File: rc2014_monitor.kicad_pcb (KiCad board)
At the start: 2 copper layers, 99.1 x 49.9 mm, 51 parts, among them J1 Z80 Bus, J2 Pro Bus, J3 USB_B_Micro, J4 M3 Mounting Hole, SW1 Line Selection, SW2 SW_Push, SW3 Step, SW4 Run/Step Mode, U1 74HCT138, U10 LMC555xM, U11 74HCT00, U12 74HCT74, U2 74HCT151, U3 74HCT541, U4 74HCT541, U5 74HCT541, U6 74HCT32, U7 MAX40200AUK, U8 MAX40200AUK, U9 DS1813R-5+T&R

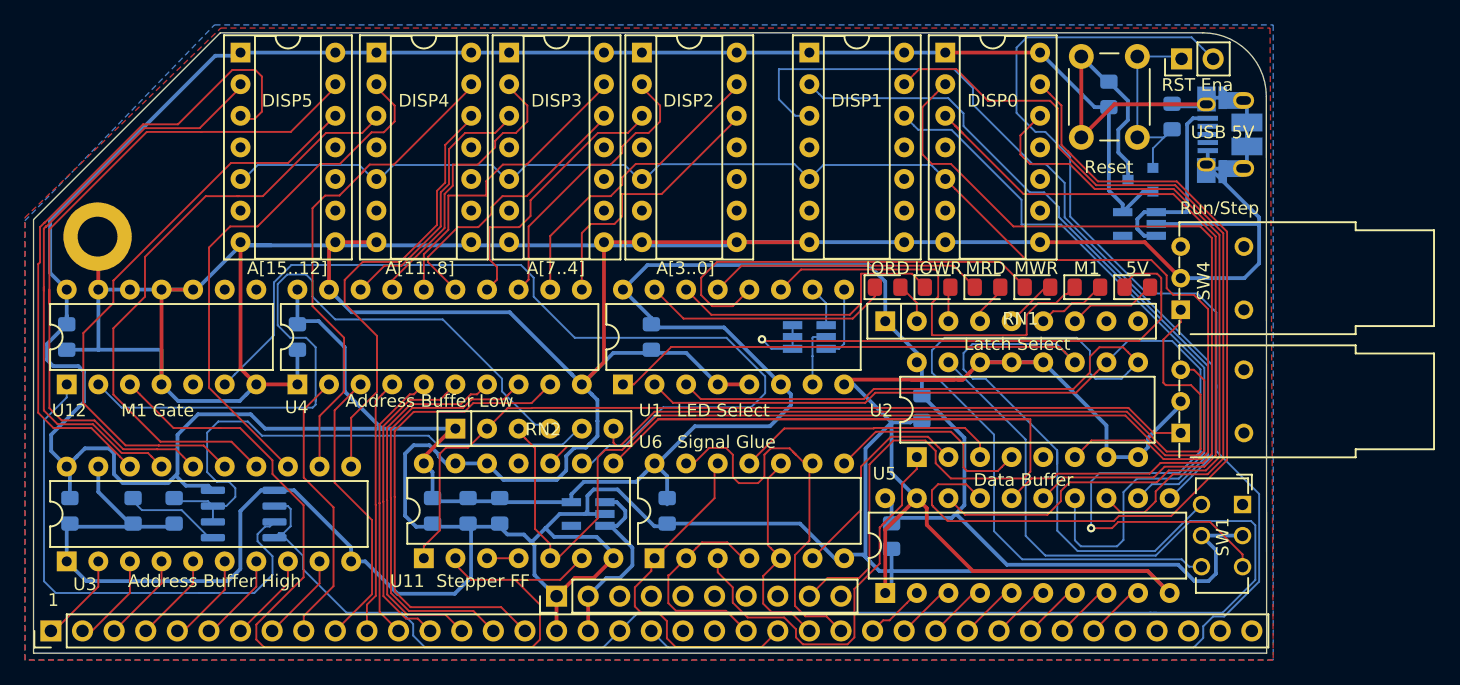
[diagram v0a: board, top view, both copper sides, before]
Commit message: fixed some alignments
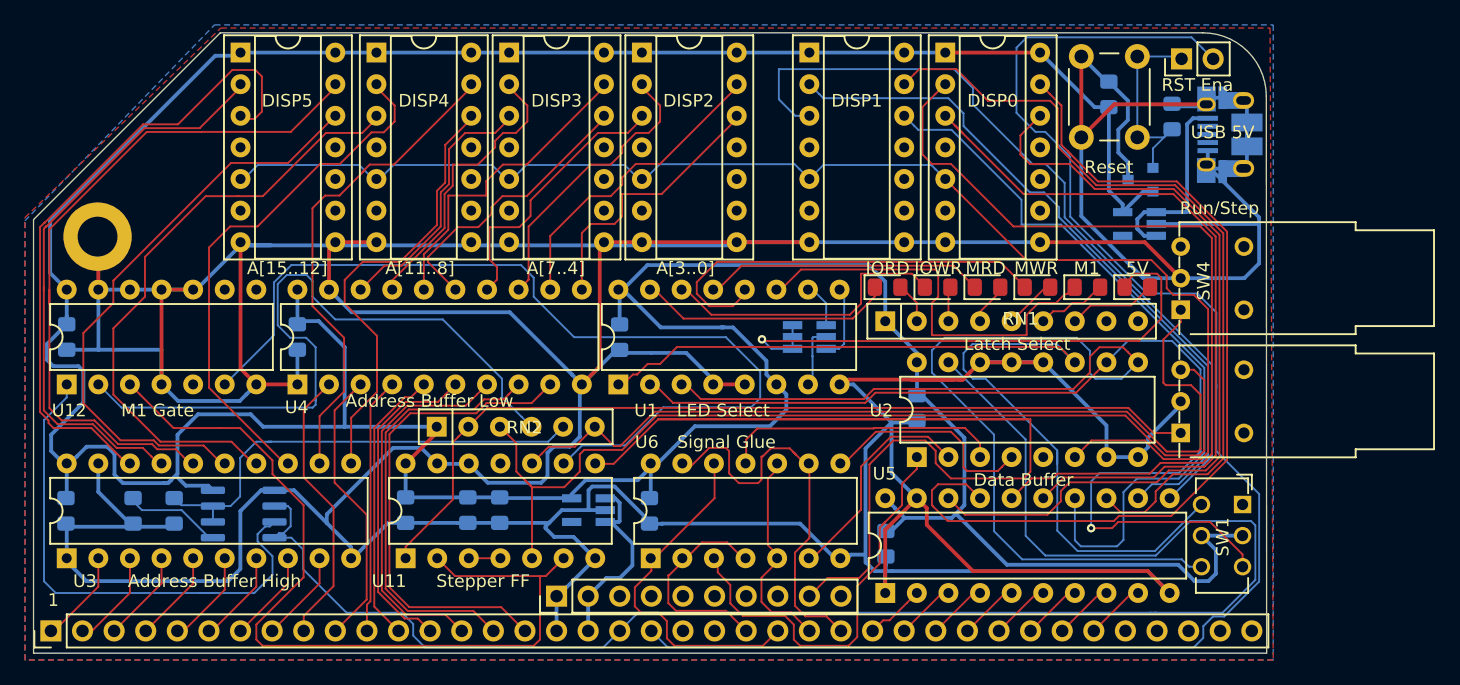
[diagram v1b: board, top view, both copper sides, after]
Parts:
- moved C13 2.55 mm to (123.3, 101.9)
- moved C14 2.17 mm to (106.1, 115.8)
- moved RN2 1.51 mm to (108.6, 109.1)
- moved U11 1.46 mm to (106.1, 119.6)
- moved C6 1.42 mm to (125.7, 115.8)
- moved C5 0.76 mm to (144.7, 118.5)
- moved C2 0.40 mm to (147.2, 107.6)
- moved U1 0.37 mm to (123.2, 105.7)
- moved C3 0.32 mm to (78.8, 115.8)
- moved U8 0.31 mm to (120.8, 115.8)
- moved U6 0.31 mm to (125.8, 119.6)
- moved U3 0.25 mm to (78.9, 119.6)
- moved C8 0.06 mm to (111.1, 115.8)
- moved C7 0.06 mm to (113.7, 115.8)
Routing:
- net U10_7: track 45.2 -> 37.5 mm
- net +5V: track 335.2 -> 337.7 mm
- net U11A_5: track 81.6 -> 79.1 mm
- net U12A_2: track 59.2 -> 57.7 mm
- net Net-(U11-Pad2): track 72.1 -> 70.8 mm
- net IO_WR: track 21.7 -> 23.0 mm
- net ~WAIT: track 99.1 -> 100.3 mm
- net GND: track 589.8 -> 588.8 mm
- net U11A_1: track 70.8 -> 71.6 mm
- net M_WR: track 32.7 -> 33.4 mm
- net Net-(U11-Pad9): track 73.4 -> 74.1 mm

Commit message: more fixes
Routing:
- net ~WAIT: track 100.3 -> 75.7 mm
- net Net-(U11-Pad2): track 70.8 -> 72.1 mm
- net U11C_10: track 72.3 -> 71.1 mm
- net D_A12: track 47.5 -> 47.0 mm

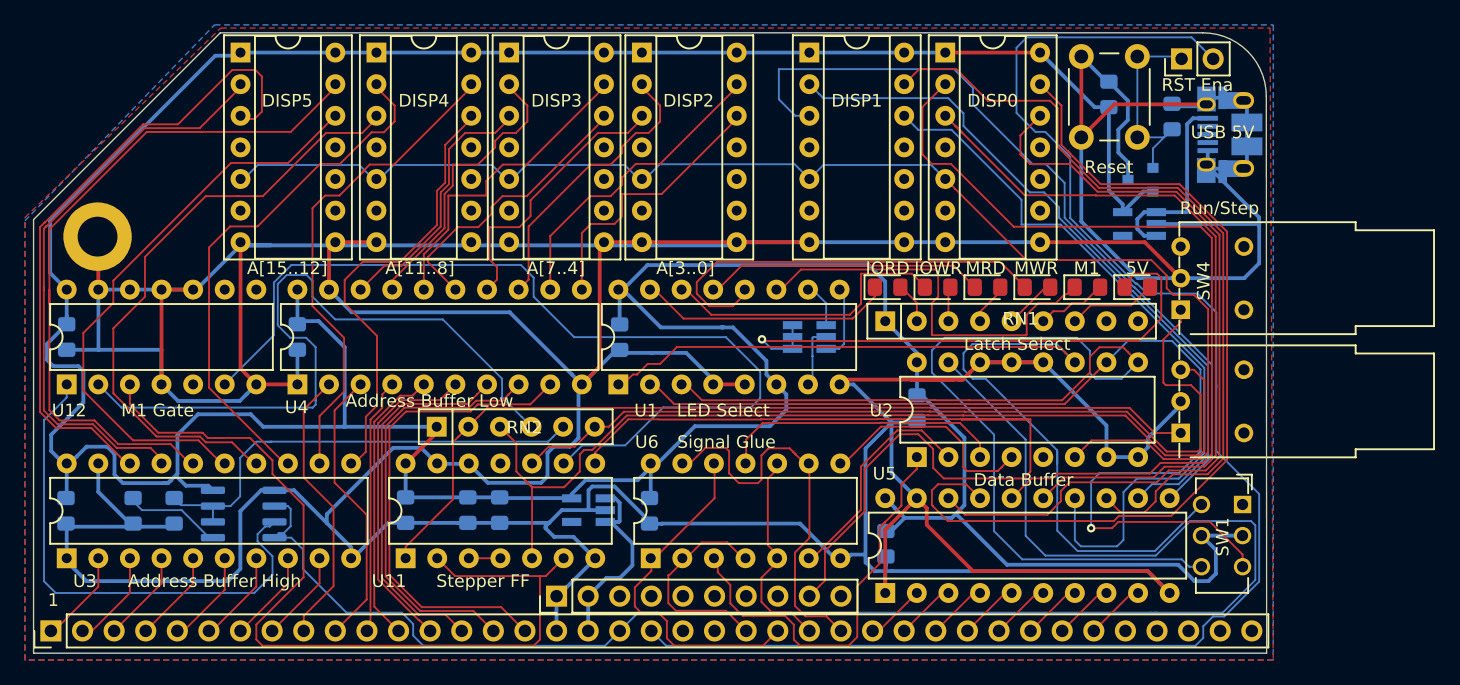
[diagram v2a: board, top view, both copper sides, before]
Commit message: use reset to clear the displays
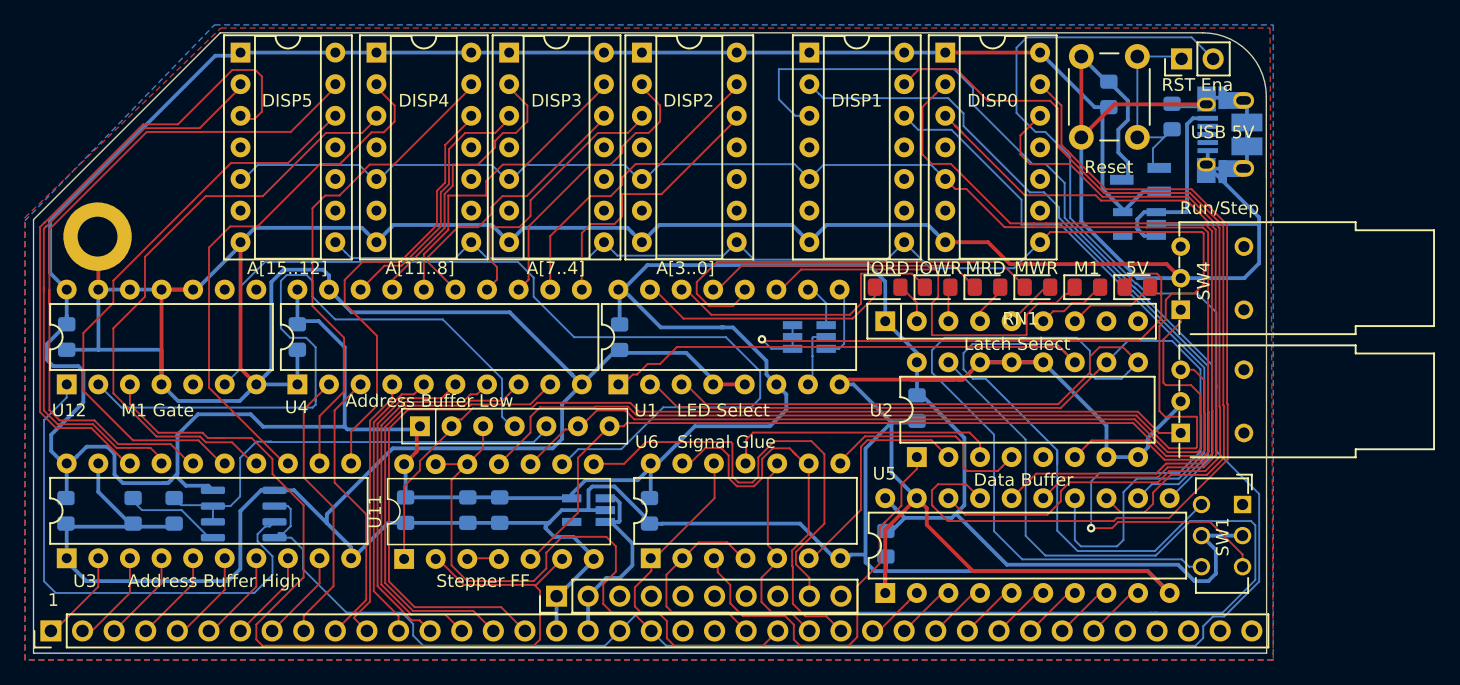
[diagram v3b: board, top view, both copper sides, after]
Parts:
- removed ?: , 
- RN2: footprint Resistor_THT:R_Array_SIP6 -> Resistor_THT:R_Array_SIP7
- U9: footprint Package_TO_SOT_SMD:SOT-23 -> Package_TO_SOT_SMD:SOT-23_Handsoldering
- moved RN2 1.35 mm to (107.3, 109.0)
- moved U11 0.13 mm to (106.0, 119.7)
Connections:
- net U10_7 renamed RN2_4
- net U11A_1 renamed RN2_1
- net U11C_10 renamed RN2_5
- net U12A_2 renamed RN2_3
- DISP0 pad 8: GND -> CLR
- DISP1 pad 8: GND -> CLR
- DISP2 pad 8: GND -> CLR
- DISP3 pad 8: GND -> CLR
- DISP4 pad 8: GND -> CLR
- DISP5 pad 8: GND -> CLR
- J1 pad 20: ~RESET -> RN2_2
- JP5 pad 2: ~RESET -> RN2_2
- RN2 pad 3: U11A_5 -> RN2_2
- SW3 pad 3: U11A_5 -> RN2_6
- U11 pad 11: (no net) -> CLR
- U11 pad 12: GND -> RN2_2
- U11 pad 13: GND -> RN2_2
- U11 pad 5: U11A_5 -> RN2_6
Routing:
- net RN2_2: track 0.00 -> 164.1 mm
- net CLR: track 0.00 -> 158.7 mm
- net ~RESET: track 123.0 -> 0.00 mm
- net U11A_5: track 79.1 -> 0.00 mm
- net RN2_6: track 0.00 -> 70.0 mm
- net ~WAIT: track 75.7 -> 37.6 mm
- net GND: track 589.0 -> 565.3 mm
- net LATCH: track 111.8 -> 114.9 mm
- net RN2_1: track 71.4 -> 73.1 mm
- net +5V: track 337.7 -> 336.1 mm
- net Net-(U11-Pad9): track 74.1 -> 75.7 mm
- net RN2_4: track 37.5 -> 36.1 mm
- net A5: track 20.7 -> 21.5 mm
- net IO_WR: track 23.3 -> 22.7 mm
- net RN2_3: track 57.7 -> 57.1 mm
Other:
- board text added: "Bus Monitor & Debugger v0.2 by Hyiger Designs"
- board text removed: "Bus Monitor & Debugger v0.1 by Hyiger Designs"

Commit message: Fixed some courtyard overlaps and rotary switch orientation
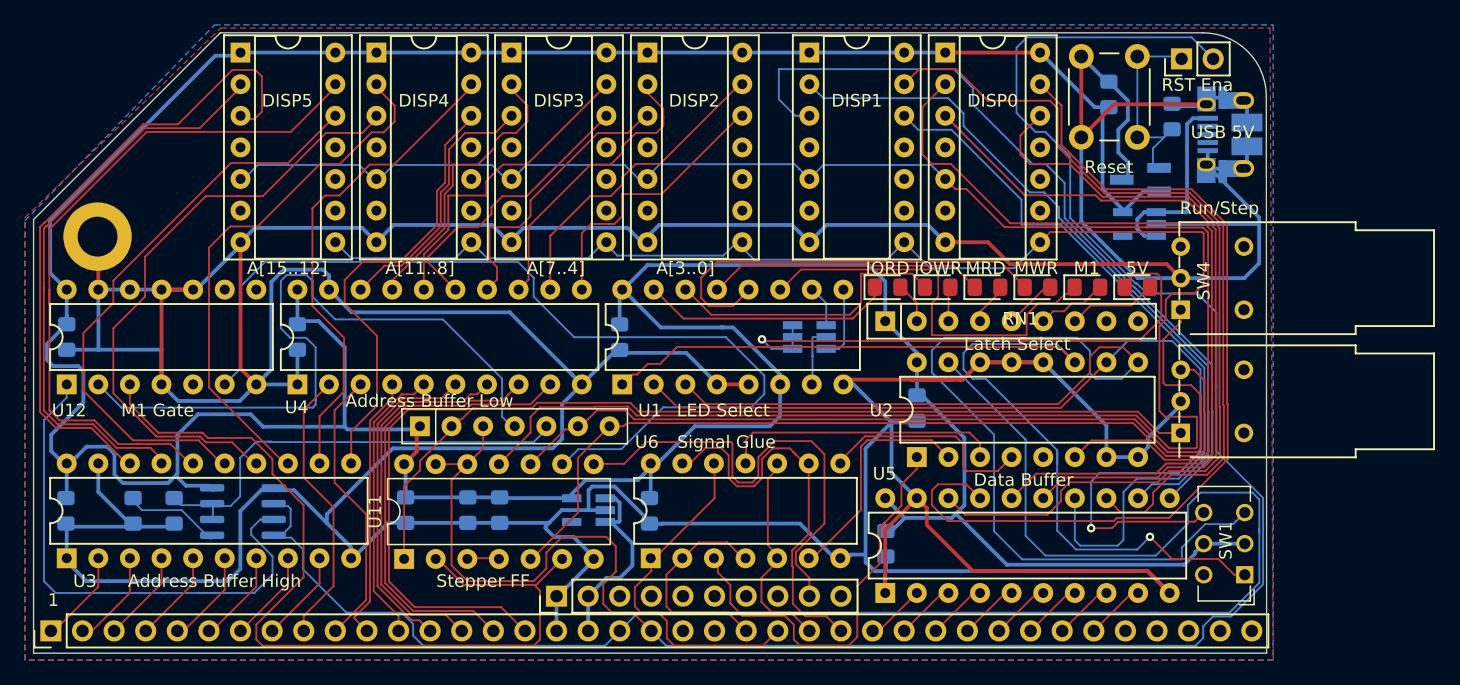
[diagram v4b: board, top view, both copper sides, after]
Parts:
- moved SW1 0.60 mm to (172.3, 118.4), turned to 180 degrees
- moved DISP2 0.45 mm to (125.5, 79.0)
- moved U1 0.31 mm to (123.5, 105.7)
- moved U10 0.20 mm to (93.0, 115.9)
- moved DISP3 0.19 mm to (114.6, 79.0)
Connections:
- SW1 pad 8: (no net) -> Net-(SW1-Pad8)
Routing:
- net Net-(SW1-Pad4): track 94.5 -> 99.9 mm
- net ~M1: track 131.4 -> 136.4 mm
- net +5V: track 336.1 -> 331.1 mm
- net Net-(SW1-Pad2): track 82.4 -> 77.6 mm
- net Net-(SW1-Pad1): track 80.7 -> 84.3 mm, vias 0 -> 1
- net Net-(U10-Pad3): track 42.6 -> 43.6 mm
- net D_A2: track 23.1 -> 23.8 mm
- net RN2_2: track 164.1 -> 164.7 mm

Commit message: changes to stepper circuit, pcb layout changes
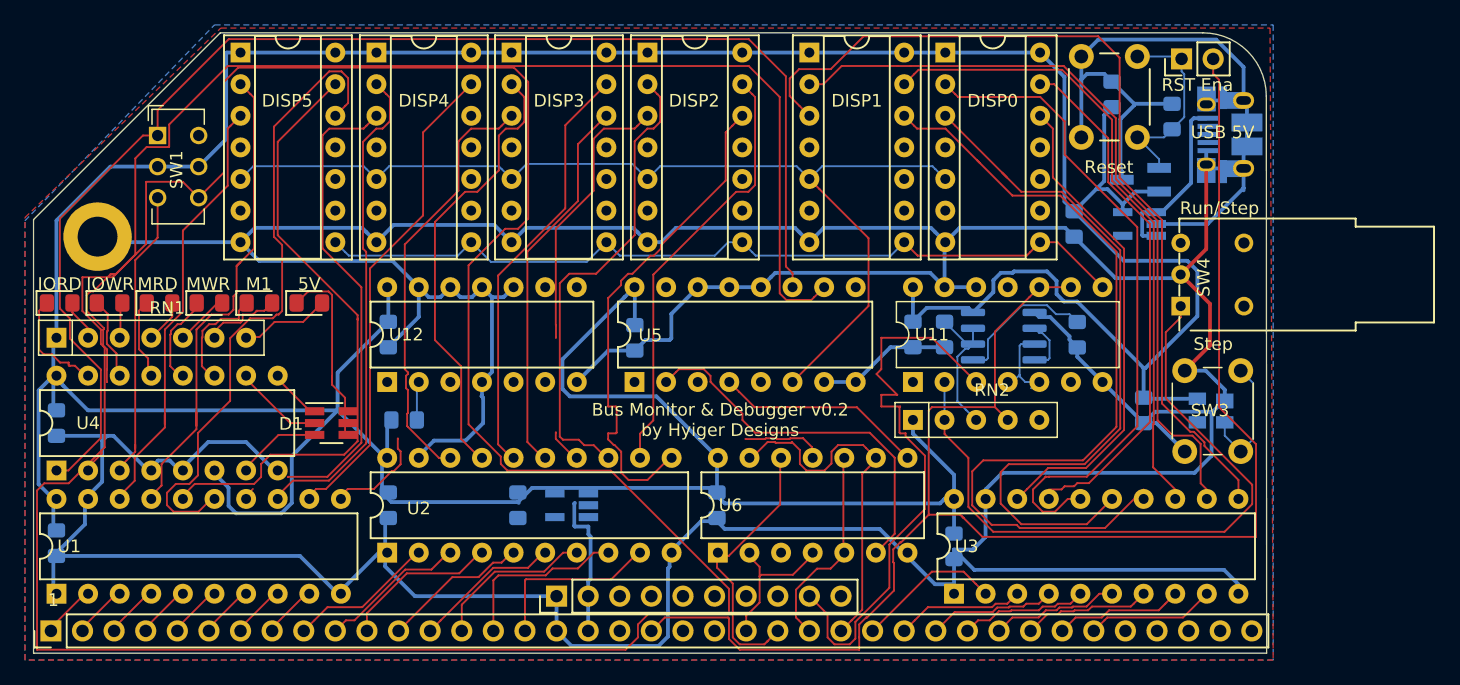
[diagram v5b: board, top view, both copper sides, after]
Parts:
- added C13: 100nF, Capacitor_SMD:C_0805_2012Metric_Pad1.15x1.40mm_HandSolder, B.Cu at (165.4, 107.7)
- added R1: 10K, Resistor_SMD:R_0805_2012Metric_Pad1.15x1.40mm_HandSolder, B.Cu at (106.0, 108.5)
- added U13: MAX6816, Package_TO_SOT_SMD:SOT-143, B.Cu at (170.8, 107.8)
- D1: moved to F.Cu
- RN1: value 270R Bussed -> 1K Bussed; footprint Resistor_THT:R_Array_SIP9 -> Resistor_THT:R_Array_SIP7
- RN2: footprint Resistor_THT:R_Array_SIP7 -> Resistor_THT:R_Array_SIP5
- SW3: value Step -> SW_Push; footprint Button_Switch_THT:SW_NKK_BB15AH -> Button_Switch_THT:SW_PUSH_6mm
- moved SW1 90.1 mm to (87.4, 88.2), turned to 0 degrees
- moved C14 77.2 mm to (160.1, 101.7)
- moved RN1 66.6 mm to (78.0, 101.9)
- moved LED4 66.6 mm to (90.3, 99.1)
- moved LED1 66.6 mm to (78.3, 99.1)
- moved LED3 66.6 mm to (86.3, 99.1)
- moved LED6 66.6 mm to (98.4, 99.1)
- moved LED2 66.6 mm to (82.3, 99.1)
- moved LED5 66.6 mm to (94.4, 99.1)
- moved C15 63.5 mm to (149.4, 101.6)
- moved U10 62.8 mm to (154.2, 101.8)
- moved C17 51.6 mm to (159.8, 92.8)
- moved U4 46.0 mm to (78.0, 112.6)
- moved U11 43.3 mm to (146.9, 105.5)
- moved C2 42.9 mm to (104.7, 101.6)
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- renumbered C13 to C11, C14 to C12, C11 to C14, C12 to C15, C7 to C17, C9 to C7, C10 to C9, U3 to U1, U4 to U2, U5 to U3, U1 to U4, U2 to U5
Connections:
- C15 pad 1: RN2_4 -> RN2_3
- DISP0 pad 8: CLR -> RESET
- DISP1 pad 8: CLR -> RESET
- DISP2 pad 8: CLR -> RESET
- DISP3 pad 8: CLR -> RESET
- DISP4 pad 8: CLR -> RESET
- DISP5 pad 8: CLR -> RESET
- J1 pad 20: RN2_2 -> RN2_1
- JP5 pad 2: RN2_2 -> RN2_1
- RN2 pad 2: RN2_1 -> RN2_4
- RN2 pad 3: RN2_2 -> RN2_3
- RN2 pad 4: RN2_3 -> RN2_1
- RN2 pad 5: RN2_4 -> (no net)
- SW1 pad 8: Net-(SW1-Pad8) -> (no net)
- SW3 pad 1: RN2_1 -> GND
- SW3 pad 2: GND -> Net-(SW3-Pad2)
- SW4 pad 1: RN2_5 -> RN2_4
- U10 pad 6: RN2_4 -> RN2_3
- U10 pad 7: RN2_4 -> RN2_3
- U11 pad 1: RN2_1 -> Net-(U11-Pad1)
- U11 pad 10: RN2_5 -> RN2_1
- U11 pad 11: CLR -> (no net)
- U11 pad 12: RN2_2 -> GND
- U11 pad 13: RN2_2 -> GND
- U11 pad 2: Net-(U11-Pad2) -> RN2_4
- U11 pad 3: Net-(U11-Pad3) -> ~WAIT
- U11 pad 4: Net-(U11-Pad3) -> Net-(U10-Pad3)
- U11 pad 5: RN2_6 -> Net-(U10-Pad3)
- U11 pad 6: Net-(U11-Pad2) -> Net-(U11-Pad6)
- U11 pad 8: ~WAIT -> RESET
- U11 pad 9: Net-(U11-Pad9) -> RN2_1
- U12 pad 1: Net-(U10-Pad3) -> Net-(U11-Pad6)
- U12 pad 2: RN2_3 -> Net-(R1-Pad2)
- U12 pad 3: Net-(U11-Pad2) -> Net-(U12-Pad3)
- U12 pad 6: Net-(U11-Pad9) -> Net-(U11-Pad1)
- U4 pad 10: Net-(D1-Pad1) -> Net-(D1-Pad2)
- U4 pad 7: Net-(D1-Pad2) -> Net-(D1-Pad3)
- U4 pad 9: Net-(D1-Pad3) -> Net-(D1-Pad1)
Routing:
- net Net-(SW1-Pad2): track 77.6 -> 302.1 mm, vias 1 -> 0
- net RN2_2: track 164.7 -> 0.00 mm
- net CLR: track 158.7 -> 0.00 mm
- net ~M1: track 136.4 -> 4.31 mm
- net Net-(SW1-Pad4): track 99.9 -> 23.6 mm
- net Net-(U11-Pad9): track 75.9 -> 0.00 mm
- net GND: track 565.3 -> 490.9 mm
- net Net-(U11-Pad2): track 72.1 -> 0.00 mm
- net RN2_5: track 71.1 -> 0.00 mm
- net RN2_6: track 70.0 -> 0.00 mm
- net RESET: track 0.00 -> 68.0 mm
- net RN2_1: track 73.1 -> 128.5 mm
- net RN2_3: track 57.1 -> 11.7 mm
- net Net-(U10-Pad3): track 43.6 -> 7.45 mm
- net M_WR: track 33.4 -> 0.00 mm
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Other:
- board text added: "Step"
- board text removed: "A[11..8]"
- board text removed: "A[15..12]"
- board text removed: "A[3..0]"
- board text removed: "A[7..4]"
- board text removed: "Address Buffer High"
- board text removed: "Address Buffer Low"
- board text removed: "Data Buffer"
- board text removed: "LED Select"
- board text removed: "Latch Select"
- board text removed: "M1 Edge Trigger"
- board text removed: "M1 Gate"
- board text removed: "Signal Glue"
- board text removed: "Stepper FF"

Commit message: new layout
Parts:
- moved C14 47.5 mm to (112.6, 101.4)
- moved R1 41.9 mm to (147.9, 107.7)
- moved RN2 41.7 mm to (105.2, 108.5)
- moved U11 41.7 mm to (105.2, 105.5)
- moved U12 41.2 mm to (145.9, 105.2)
- moved C15 39.6 mm to (109.8, 101.4)
- moved C11 39.4 mm to (107.5, 101.4)
- moved U10 36.1 mm to (118.1, 101.5)
- moved RN1 3.30 mm to (81.3, 101.9)
- moved LED1 0.76 mm to (79.1, 99.1)
- moved LED2 0.76 mm to (83.1, 99.1)
- moved LED3 0.76 mm to (87.1, 99.1)
- moved LED4 0.76 mm to (91.1, 99.1)
- moved LED6 0.76 mm to (99.1, 99.1)
- moved LED5 0.76 mm to (95.1, 99.1)
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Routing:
- net Net-(SW1-Pad2): track 302.1 -> 116.4 mm
- net ~M1: track 4.31 -> 127.3 mm
- net Net-(U11-Pad1): track 0.00 -> 68.4 mm
- net Net-(SW1-Pad4): track 23.6 -> 84.5 mm
- net M_WR: track 0.00 -> 35.7 mm
- net Net-(U11-Pad6): track 0.00 -> 30.3 mm
- net Net-(U12-Pad3): track 0.00 -> 28.8 mm
- net D_A8: track 8.38 -> 35.5 mm
- net GND: track 490.9 -> 517.5 mm
- net RN2_4: track 54.7 -> 74.6 mm
- net RN2_1: track 128.5 -> 145.3 mm
- net +5V: track 358.4 -> 372.3 mm
- net RN2_3: track 11.7 -> 23.6 mm
- net ~WAIT: track 46.9 -> 39.2 mm
- net D_A3: track 25.0 -> 32.6 mm
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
